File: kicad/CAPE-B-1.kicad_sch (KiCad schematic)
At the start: 18 parts

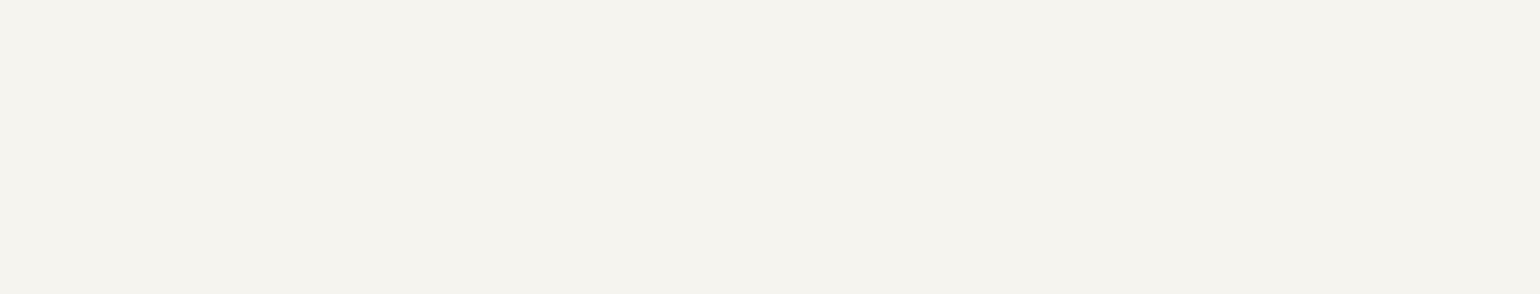
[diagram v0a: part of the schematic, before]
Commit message: Add magnetometer, battery monitor, SBUS/XCVR mux to Cape-A/B; update v2 EMI variants
Cape-A-1.kicad_sch (via add_sensors_sbus.py):
- QMC5883L 3-axis magnetometer on I2C1 with GPIO_MAG_DRDY output
- INA219AIDR battery voltage monitor on I2C1 (voltage-only, IN+/IN- tied)
- J_VBAT JST GH 2P connector for VBAT_MON_P/GND
- J_SBUS JST GH 3P → 100R R_SBUS → 74LVC1G14 Schmitt inverter → UART_SBUS_RX
  (SBUS is inverted UART 100kbaud 8E2; inverter restores standard logic)

Cape-B-1.kicad_sch (via add_sensors_sbus.py):
- J_XCVR JST GH 6P shared connector (GND/+5V/TX/RX_RAW/PTT_N/+3V3)
- 74LVC1G14 U_SBUS_B inverter on XCVR_RX_RAW → SBUS_INV_RX
- SW1 2-position DIP switch: SW1-1=XCVR direct path, SW1-2=SBUS inverted path
- R_XCVR_RX / R_SBUS_RX 100R series resistors prevent bus contention
- Same UART_RCRS_TX/RX signals used for both modes

gen_cape_a2.py:
- QMC5883L → MMC5983MA (MEMSIC AEC-Q100 18-bit, same I2C interface)
- INA219AIDR → INA226AIDGSR (TI 16-bit 36V, VSSOP-8; VS pin remapped)
- D_SBUS_TVS (PRTR5V0U2X) added on SBUS_RAW for ESD/EMI clamp

gen_cape_b2.py:
- D_XCVR_TVS (PRTR5V0U2X) added on XCVR_RX_RAW for 49 MHz antenna ESD clamp
- Fixed remove_sexp_block trailing-whitespace bug: was consuming leading indent of
  next block, causing alternating global_label patterns to go unmatched; now only
  consumes \r\n, not spaces — all PHY label removals now pass sanity check

All four schematics regenerated; all sanity checks pass (CAPE-A-2 and CAPE-B-2).

https://claude.ai/code/session_013nvDzZZt6Rta9diEyt3XAh
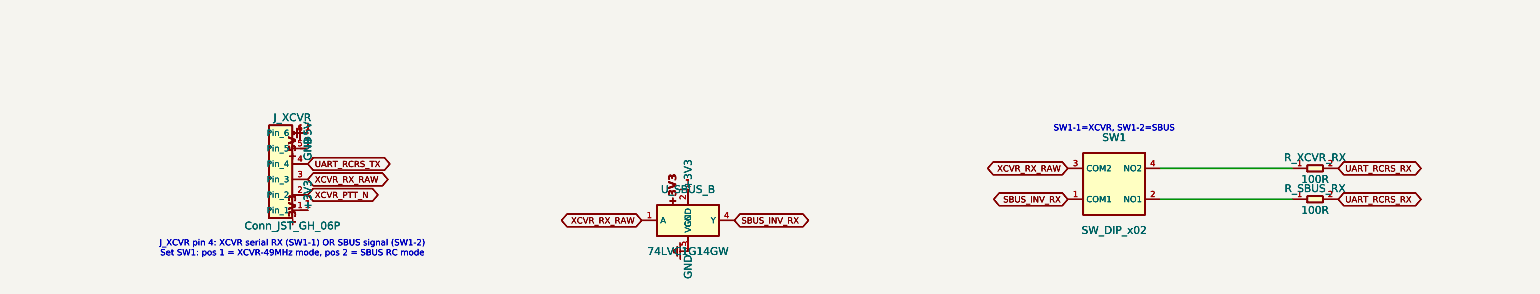
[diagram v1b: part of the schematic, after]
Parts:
- added J_XCVR: Conn_JST_GH_06P, Connector_JST:JST_GH_SM06B-GHS-TB_1x06-1MP_P1.25mm_Horizontal, symbol Conn_JST_GH_06P
- added R_SBUS_RX, R_XCVR_RX: 100R, Resistor_SMD:R_0402_1005Metric, symbol R_SMD
- added SW1: SW_DIP_x02, Package_DIP:DIP-4_W7.62mm, symbol SW_DIP_x02
- added U_SBUS_B: 74LVC1G14GW, Package_TO_SOT_SMD:SOT-23-5, symbol 74LVC1G14
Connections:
- net +3V3: now also J_XCVR.1 (Pin_1), U_SBUS_B.2 (GND)
- net +5V: now also J_XCVR.5 (Pin_5)
- net GND: now also J_XCVR.6 (Pin_6), U_SBUS_B.5 (VCC)
- net UART_RCRS_RX: now also R_SBUS_RX.2, R_XCVR_RX.2
- net UART_RCRS_TX: now also J_XCVR.4 (Pin_4)
- new net: R_SBUS_RX.1, SW1.2 (NO1)
- new net: R_XCVR_RX.1, SW1.4 (NO2)
- new net SBUS_INV_RX: SW1.1 (COM1), U_SBUS_B.4 (Y)
- new net XCVR_PTT_N: J_XCVR.2 (Pin_2)
- new net XCVR_RX_RAW: J_XCVR.3 (Pin_3), SW1.3 (COM2), U_SBUS_B.1 (A)
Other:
- note added: "J_XCVR pin 4: XCVR serial RX (SW1-1) OR SBUS signal (SW1-2) Set SW1: pos 1 = XCVR-49MHz mode, pos 2 = SBUS RC mode"
- note added: "SW1-1=XCVR, SW1-2=SBUS"
